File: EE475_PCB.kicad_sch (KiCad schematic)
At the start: 11 parts, among them J1 Conn_01x15_Female, J2 Conn_01x02_Female, J3 Conn_01x15_Female, J4 Conn_01x02_Female, Q1 S8050, Q2 S8050

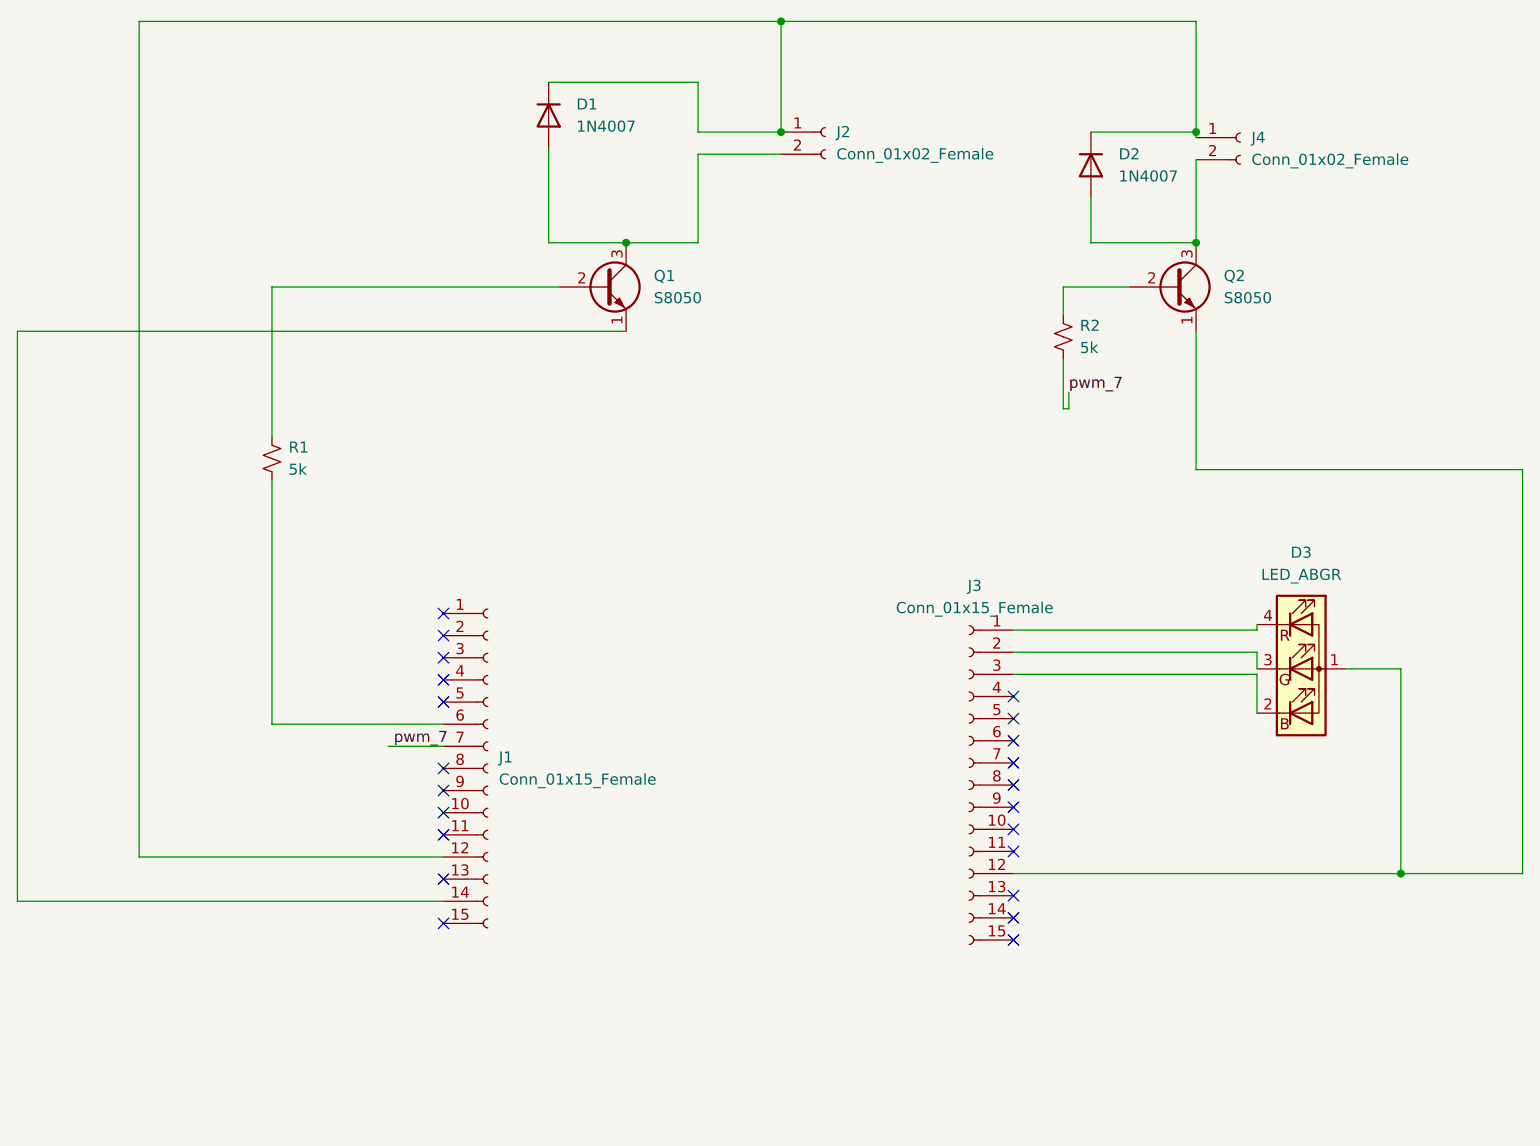
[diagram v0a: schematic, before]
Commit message: Updated Schematic of motor hub with power supply width
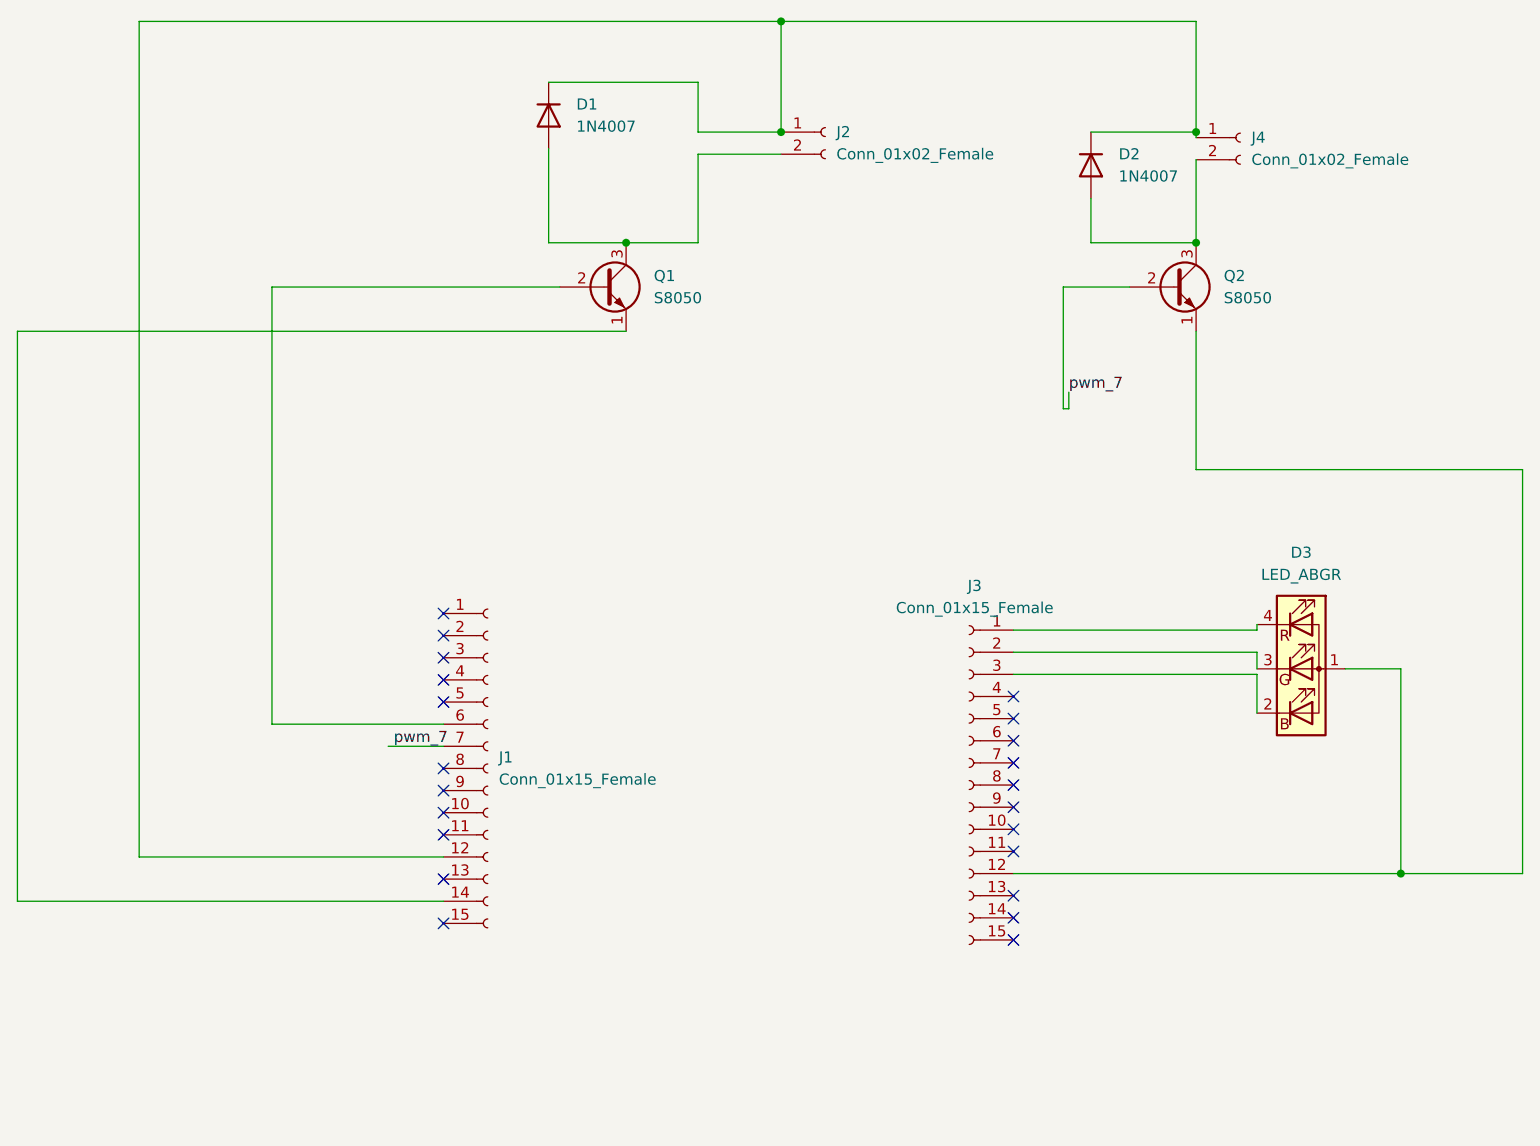
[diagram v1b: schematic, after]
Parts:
- removed R1, R2: 5k, Resistor_SMD:R_0402_1005Metric, symbol Device:R_Small_US
- J2, J4: footprint (none) -> Connector_PinSocket_2.54mm:PinSocket_1x02_P2.54mm_Vertical
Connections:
- net pwm_7: now also Q2.2 (B)
- net at Q1.2 (B): now also J1.6 (Pin_6)
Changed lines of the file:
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@@
-    (stroke (width 0) (type default) (color 0 0 0 0))
-  )
-  (wire (pts (xy 179.07 55.88) (xy 179.07 59.055))
     (stroke (width 0) (type default) (color 0 0 0 0))
   )
@@
     (stroke (width 0) (type default) (color 0 0 0 0))
   )
-  (wire (pts (xy 179.07 69.85) (xy 179.07 64.135))
+  (wire (pts (xy 179.07 55.88) (xy 179.07 69.85))
     (stroke (width 0) (type default) (color 0 0 0 0))
   )
@@
     (stroke (width 0) (type default) (color 0 0 0 0))
   )
-  (wire (pts (xy 88.265 78.105) (xy 88.265 106.045))
+  (wire (pts (xy 88.265 55.88) (xy 88.265 106.045))
     (stroke (width 0) (type default) (color 0 0 0 0))
   )
@@
   )
   (wire (pts (xy 107.95 126.365) (xy 59.055 126.365))
-    (stroke (width 0) (type default) (color 0 0 0 0))
-  )
-  (wire (pts (xy 88.265 55.88) (xy 88.265 73.025))
     (stroke (width 0) (type default) (color 0 0 0 0))
   )
@@
   (label "pwm_7" (at 102.235 108.585 0)
     (effects (font (size 1.27 1.27)) (justify left bottom))
-  )
-  (symbol (lib_id "Device:R_Small_US") (at 179.07 61.595 0) (unit 1)
-    (in_bom yes) (on_board yes) (fields_autoplaced)
-    (property "Reference" "R2" (id 0) (at 180.975 60.3249 0)
-      (effects (font (size 1.27 1.27)) (justify left))
-    )
-    (property "Value" "5k" (id 1) (at 180.975 62.8649 0)
-      (effects (font (size 1.27 1.27)) (justify left))
-    )
-    (property "Footprint" "Resistor_SMD:R_0402_1005Metric" (id 2) (at 179.07 61.595 0)
-      (effects (font (size 1.27 1.27)) hide)
-    )
-    (property "Datasheet" "~" (id 3) (at 179.07 61.595 0)
-      (effects (font (size 1.27 1.27)) hide)
-    )
-    (pin "1")
-    (pin "2")
   )
   (symbol (lib_id "Transistor_BJT:S8050") (at 126.365 55.88 0) (unit 1)
@@
       (effects (font (size 1.27 1.27)) (justify left))
     )
-    (property "Footprint" "" (id 2) (at 199.39 38.735 0)
+    (property "Footprint" "Connector_PinSocket_2.54mm:PinSocket_1x02_P2.54mm_Vertical" (id 2) (at 199.39 38.735 0)
       (effects (font (size 1.27 1.27)) hide)
     )
@@
       (effects (font (size 1.27 1.27)) (justify left))
     )
-    (property "Footprint" "" (id 2) (at 151.765 38.1 0)
+    (property "Footprint" "Connector_PinSocket_2.54mm:PinSocket_1x02_P2.54mm_Vertical" (id 2) (at 151.765 38.1 0)
       (effects (font (size 1.27 1.27)) hide)
     )
@@
     (pin "3")
   )
-  (symbol (lib_id "Device:R_Small_US") (at 88.265 75.565 0) (unit 1)
-    (in_bom yes) (on_board yes) (fields_autoplaced)
-    (property "Reference" "R1" (id 0) (at 90.17 74.2949 0)
-      (effects (font (size 1.27 1.27)) (justify left))
-    )
-    (property "Value" "5k" (id 1) (at 90.17 76.8349 0)
-      (effects (font (size 1.27 1.27)) (justify left))
-    )
-    (property "Footprint" "Resistor_SMD:R_0402_1005Metric" (id 2) (at 88.265 75.565 0)
-      (effects (font (size 1.27 1.27)) hide)
-    )
-    (property "Datasheet" "~" (id 3) (at 88.265 75.565 0)
-      (effects (font (size 1.27 1.27)) hide)
-    )
-    (pin "1")
-    (pin "2")
-  )
   (sheet_instances
     (path "/" (page "1"))
@@
     )
     (path "/b6ce3de8-74e3-4d01-b190-d0274582e099"
-      (reference "J2") (unit 1) (value "Conn_01x02_Female") (footprint "")
+      (reference "J2") (unit 1) (value "Conn_01x02_Female") (footprint "Connector_PinSocket_2.54mm:PinSocket_1x02_P2.54mm_Vertical")
     )
     (path "/d09b42b3-a1d3-4700-b9ed-e9258430cad0"
@@
     )
     (path "/7d8d3fcc-1fb1-4da8-b4f9-db58981f1c77"
-      (reference "J4") (unit 1) (value "Conn_01x02_Female") (footprint "")
+      (reference "J4") (unit 1) (value "Conn_01x02_Female") (footprint "Connector_PinSocket_2.54mm:PinSocket_1x02_P2.54mm_Vertical")
     )
     (path "/41cec304-98be-4691-a921-3c7db05a2fbc"
@@
       (reference "Q2") (unit 1) (value "S8050") (footprint "Package_TO_SOT_THT:TO-92_Inline")
     )
-    (path "/e4e04b21-da7c-43e7-9df2-60b835121050"
-      (reference "R1") (unit 1) (value "5k") (footprint "Resistor_SMD:R_0402_1005Metric")
-    )
-    (path "/2e0aecff-257c-48af-a6e9-878ecd2c7240"
-      (reference "R2") (unit 1) (value "5k") (footprint "Resistor_SMD:R_0402_1005Metric")
-    )
-  )
+  )

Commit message: Final design of the PCB baord for Motor Controller
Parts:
- added J5, J6, J7, J8: Conn_01x02_Female, Connector_PinSocket_2.54mm:PinSocket_1x02_P2.54mm_Vertical, symbol Connector:Conn_01x02_Female
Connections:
- net at J1.14 (Pin_14), Q1.1 (E): now also J5.2 (Pin_2), J6.2 (Pin_2)
- net at D1.1 (K), D2.1 (K), J2.1 (Pin_1)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: now also J5.1 (Pin_1), J6.1 (Pin_1); no longer J1.12 (Pin_12)
- no-connect marks 22 -> 27
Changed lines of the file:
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@@
   (junction (at 194.31 50.8) (diameter 0) (color 0 0 0 0)
   )
+  (junction (at 78.74 126.365) (diameter 0) (color 0 0 0 0)
+  )
   (junction (at 128.905 50.8) (diameter 0) (color 0 0 0 0)
   )
+  (junction (at 73.025 138.43) (diameter 0) (color 0 0 0 0)
+  )
   (junction (at 194.31 38.1) (diameter 0) (color 0 0 0 0)
   )
@@
   (junction (at 146.685 38.1) (diameter 0) (color 0 0 0 0)
   )
+  (junction (at 85.09 126.365) (diameter 0) (color 0 0 0 0)
+  )
   (no_connect (at 107.95 118.745))
+  (no_connect (at 126.365 140.335))
+  (no_connect (at 107.95 121.285))
   (no_connect (at 107.95 98.425))
   (no_connect (at 107.95 123.825))
   (no_connect (at 173.355 113.03))
+  (no_connect (at 126.365 148.59))
   (no_connect (at 173.355 105.41))
   (no_connect (at 173.355 115.57))
+  (no_connect (at 126.365 151.13))
   (no_connect (at 173.355 130.81))
   (no_connect (at 173.355 120.65))
@@
   (no_connect (at 173.355 118.11))
   (no_connect (at 173.355 125.73))
+  (no_connect (at 126.365 137.795))
   (no_connect (at 107.95 111.125))
   (no_connect (at 173.355 107.95))
@@
     (stroke (width 0) (type default) (color 0 0 0 0))
   )
+  (wire (pts (xy 78.74 126.365) (xy 59.055 126.365))
+    (stroke (width 0) (type default) (color 0 0 0 0))
+  )
+  (wire (pts (xy 73.025 138.43) (xy 90.17 138.43))
+    (stroke (width 0) (type default) (color 0 0 0 0))
+  )
+  (wire (pts (xy 85.09 140.97) (xy 85.09 126.365))
+    (stroke (width 0) (type default) (color 0 0 0 0))
+  )
+  (wire (pts (xy 85.09 126.365) (xy 78.74 126.365))
+    (stroke (width 0) (type default) (color 0 0 0 0))
+  )
   (wire (pts (xy 59.055 60.96) (xy 128.905 60.96))
     (stroke (width 0) (type default) (color 0 0 0 0))
@@
     (stroke (width 0) (type default) (color 0 0 0 0))
   )
+  (wire (pts (xy 78.74 151.13) (xy 78.74 126.365))
+    (stroke (width 0) (type default) (color 0 0 0 0))
+  )
   (wire (pts (xy 128.905 50.8) (xy 120.015 50.8))
     (stroke (width 0) (type default) (color 0 0 0 0))
   )
+  (wire (pts (xy 90.17 140.97) (xy 85.09 140.97))
+    (stroke (width 0) (type default) (color 0 0 0 0))
+  )
+  (wire (pts (xy 73.025 148.59) (xy 73.025 138.43))
+    (stroke (width 0) (type default) (color 0 0 0 0))
+  )
   (wire (pts (xy 179.07 55.88) (xy 179.07 69.85))
     (stroke (width 0) (type default) (color 0 0 0 0))
@@
     (stroke (width 0) (type default) (color 0 0 0 0))
   )
-  (wire (pts (xy 73.025 25.4) (xy 73.025 121.285))
+  (wire (pts (xy 73.025 25.4) (xy 73.025 138.43))
+    (stroke (width 0) (type default) (color 0 0 0 0))
+  )
+  (wire (pts (xy 89.535 148.59) (xy 73.025 148.59))
     (stroke (width 0) (type default) (color 0 0 0 0))
   )
@@
     (stroke (width 0) (type default) (color 0 0 0 0))
   )
-  (wire (pts (xy 73.025 121.285) (xy 107.95 121.285))
-    (stroke (width 0) (type default) (color 0 0 0 0))
-  )
   (wire (pts (xy 146.685 38.1) (xy 146.685 25.4))
     (stroke (width 0) (type default) (color 0 0 0 0))
@@
     (stroke (width 0) (type default) (color 0 0 0 0))
   )
+  (wire (pts (xy 89.535 151.13) (xy 78.74 151.13))
+    (stroke (width 0) (type default) (color 0 0 0 0))
+  )
   (wire (pts (xy 211.455 99.695) (xy 217.805 99.695))
     (stroke (width 0) (type default) (color 0 0 0 0))
   )
-  (wire (pts (xy 107.95 126.365) (xy 59.055 126.365))
+  (wire (pts (xy 107.95 126.365) (xy 85.09 126.365))
     (stroke (width 0) (type default) (color 0 0 0 0))
   )
@@
   (label "pwm_7" (at 102.235 108.585 0)
     (effects (font (size 1.27 1.27)) (justify left bottom))
+  )
+  (symbol (lib_id "Connector:Conn_01x02_Female") (at 131.445 148.59 0) (unit 1)
+    (in_bom yes) (on_board yes) (fields_autoplaced)
+    (property "Reference" "J8" (id 0) (at 132.715 148.5899 0)
+      (effects (font (size 1.27 1.27)) (justify left))
+    )
+    (property "Value" "Conn_01x02_Female" (id 1) (at 132.715 151.1299 0)
+      (effects (font (size 1.27 1.27)) (justify left))
+    )
+    (property "Footprint" "Connector_PinSocket_2.54mm:PinSocket_1x02_P2.54mm_Vertical" (id 2) (at 131.445 148.59 0)
+      (effects (font (size 1.27 1.27)) hide)
+    )
+    (property "Datasheet" "~" (id 3) (at 131.445 148.59 0)
+      (effects (font (size 1.27 1.27)) hide)
+    )
+    (pin "1")
+    (pin "2")
+  )
+  (symbol (lib_id "Connector:Conn_01x02_Female") (at 95.25 138.43 0) (unit 1)
+    (in_bom yes) (on_board yes) (fields_autoplaced)
+    (property "Reference" "J6" (id 0) (at 96.52 138.4299 0)
+      (effects (font (size 1.27 1.27)) (justify left))
+    )
+    (property "Value" "Conn_01x02_Female" (id 1) (at 96.52 140.9699 0)
+      (effects (font (size 1.27 1.27)) (justify left))
+    )
+    (property "Footprint" "Connector_PinSocket_2.54mm:PinSocket_1x02_P2.54mm_Vertical" (id 2) (at 95.25 138.43 0)
+      (effects (font (size 1.27 1.27)) hide)
+    )
+    (property "Datasheet" "~" (id 3) (at 95.25 138.43 0)
+      (effects (font (size 1.27 1.27)) hide)
+    )
+    (pin "1")
+    (pin "2")
   )
   (symbol (lib_id "Transistor_BJT:S8050") (at 126.365 55.88 0) (unit 1)
@@
     (pin "9")
   )
+  (symbol (lib_id "Connector:Conn_01x02_Female") (at 94.615 148.59 0) (unit 1)
+    (in_bom yes) (on_board yes) (fields_autoplaced)
+    (property "Reference" "J5" (id 0) (at 95.885 148.5899 0)
+      (effects (font (size 1.27 1.27)) (justify left))
+    )
+    (property "Value" "Conn_01x02_Female" (id 1) (at 95.885 151.1299 0)
+      (effects (font (size 1.27 1.27)) (justify left))
+    )
+    (property "Footprint" "Connector_PinSocket_2.54mm:PinSocket_1x02_P2.54mm_Vertical" (id 2) (at 94.615 148.59 0)
+      (effects (font (size 1.27 1.27)) hide)
+    )
+    (property "Datasheet" "~" (id 3) (at 94.615 148.59 0)
+      (effects (font (size 1.27 1.27)) hide)
+    )
+    (pin "1")
+    (pin "2")
+  )
   (symbol (lib_id "Connector:Conn_01x02_Female") (at 199.39 38.735 0) (unit 1)
     (in_bom yes) (on_board yes) (fields_autoplaced)
@@
     (pin "3")
     (pin "4")
+  )
+  (symbol (lib_id "Connector:Conn_01x02_Female") (at 131.445 137.795 0) (unit 1)
+    (in_bom yes) (on_board yes) (fields_autoplaced)
+    (property "Reference" "J7" (id 0) (at 132.715 137.7949 0)
+      (effects (font (size 1.27 1.27)) (justify left))
+    )
+    (property "Value" "Conn_01x02_Female" (id 1) (at 132.715 140.3349 0)
+      (effects (font (size 1.27 1.27)) (justify left))
+    )
+    (property "Footprint" "Connector_PinSocket_2.54mm:PinSocket_1x02_P2.54mm_Vertical" (id 2) (at 131.445 137.795 0)
+      (effects (font (size 1.27 1.27)) hide)
+    )
+    (property "Datasheet" "~" (id 3) (at 131.445 137.795 0)
+      (effects (font (size 1.27 1.27)) hide)
+    )
+    (pin "1")
+    (pin "2")
   )
   (symbol (lib_id "Connector:Conn_01x15_Female") (at 168.275 113.03 0) (mirror y) (unit 1)
@@
       (reference "J4") (unit 1) (value "Conn_01x02_Female") (footprint "Connector_PinSocket_2.54mm:PinSocket_1x02_P2.54mm_Vertical")
     )
+    (path "/62d1298f-b648-4f2a-bf74-cd0157e3c369"
+      (reference "J5") (unit 1) (value "Conn_01x02_Female") (footprint "Connector_PinSocket_2.54mm:PinSocket_1x02_P2.54mm_Vertical")
+    )
+    (path "/3e757767-e910-45c4-80d1-271d376dfe80"
+      (reference "J6") (unit 1) (value "Conn_01x02_Female") (footprint "Connector_PinSocket_2.54mm:PinSocket_1x02_P2.54mm_Vertical")
+    )
+    (path "/c16bf5c2-af45-4c6b-8e1c-7789c1db7afc"
+      (reference "J7") (unit 1) (value "Conn_01x02_Female") (footprint "Connector_PinSocket_2.54mm:PinSocket_1x02_P2.54mm_Vertical")
+    )
+    (path "/0f53b950-e83f-4aa5-bd5e-2d063c9dddd4"
+      (reference "J8") (unit 1) (value "Conn_01x02_Female") (footprint "Connector_PinSocket_2.54mm:PinSocket_1x02_P2.54mm_Vertical")
+    )
     (path "/41cec304-98be-4691-a921-3c7db05a2fbc"
